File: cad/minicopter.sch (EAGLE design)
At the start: 39 parts, among them CN2 DO NOT PLACE, U1 STM32F411/48, U2 LSM6DS3, U3 DRV8839, U4 LPS25HB, U5 DRV8839, U6 LIS3MDL

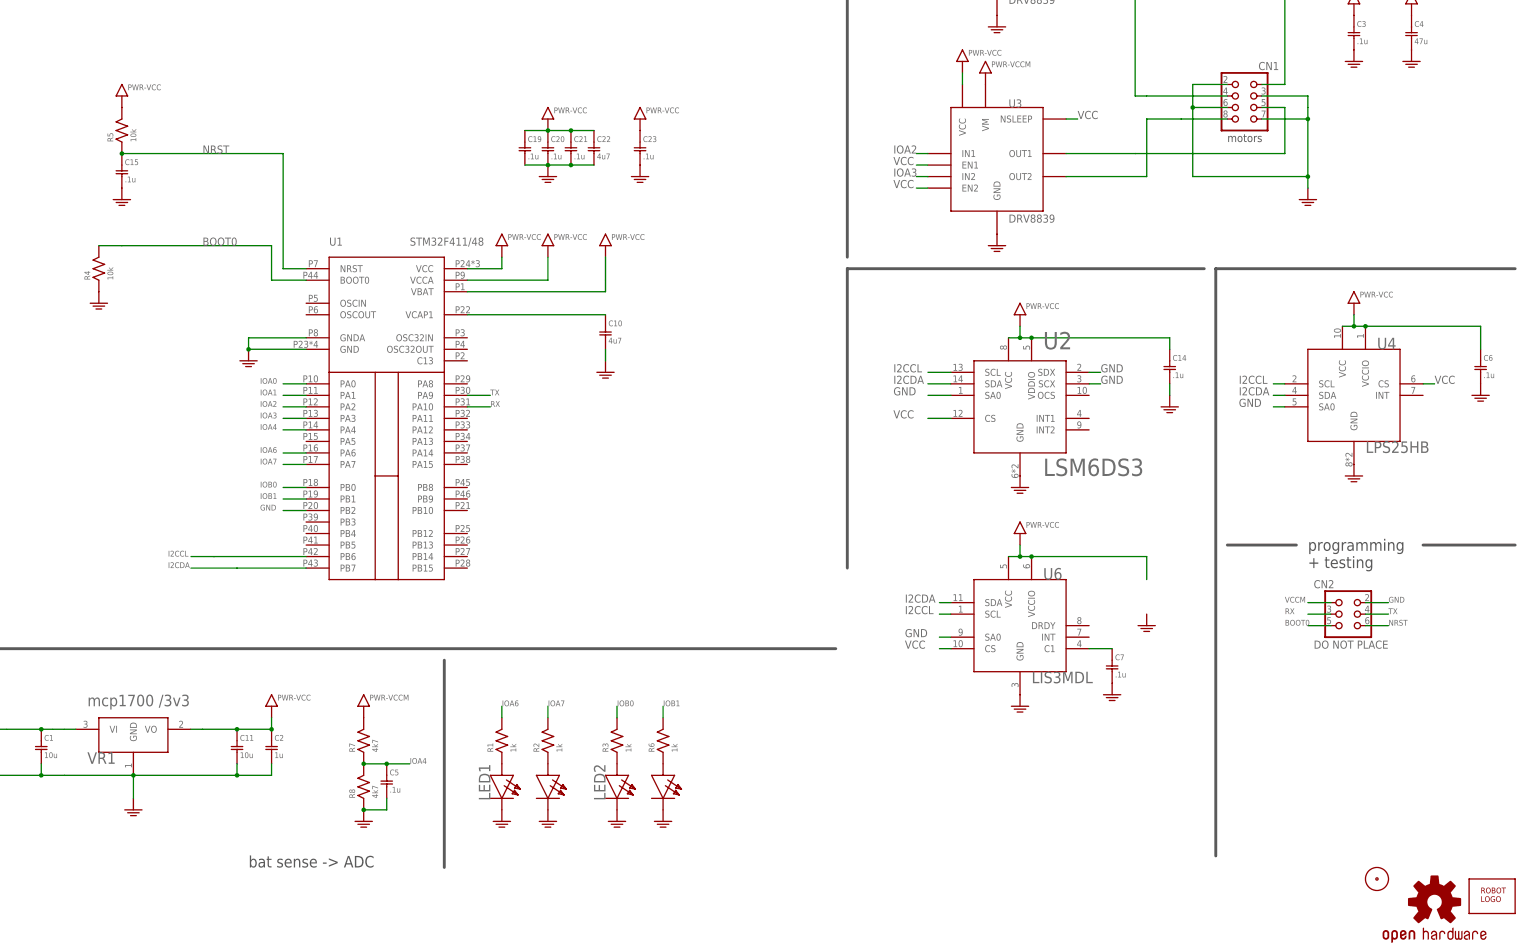
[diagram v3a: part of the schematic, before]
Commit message: add piezo
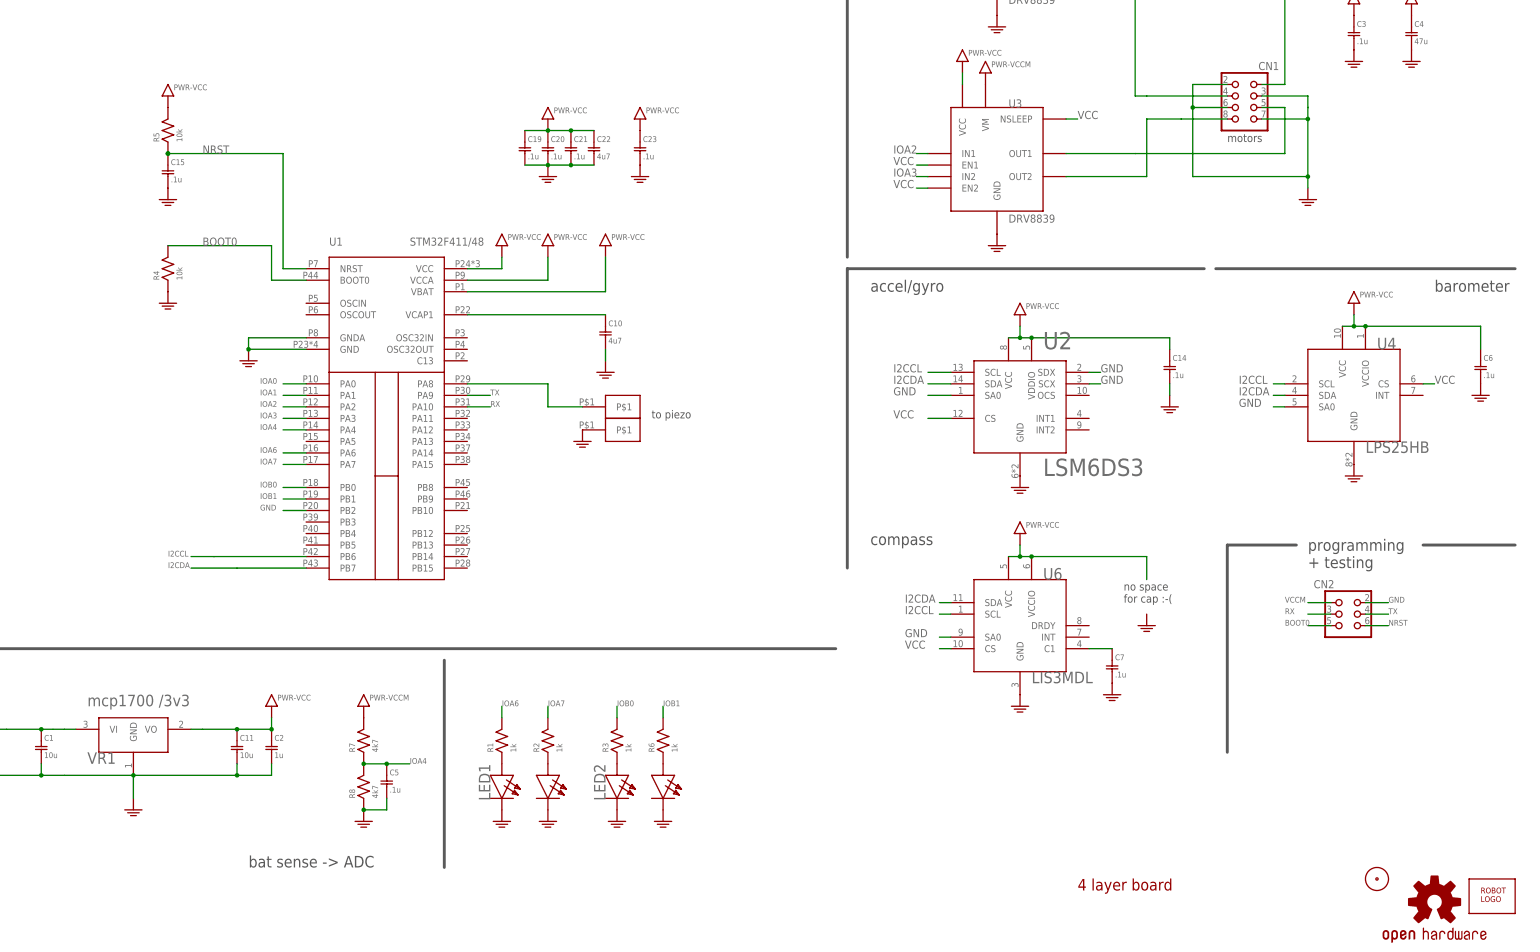
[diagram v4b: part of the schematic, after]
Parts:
- added CN4, CN5: HEADER-1X1SMALL, jaw:HEADER-1X1SMALL
- CN2: value DO NOT PLACE -> HEADER-3X2-PTH
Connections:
- new net PZ0: CN4.P$1, U1.PA8
- net GND: now also CN5.P$1
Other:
- note added: "4 layer board"
- note added: "accel/gyro"
- note added: "barometer"
- note added: "compass"
- note added: "no space for cap :-("
- note added: "to piezo"
- moved on the sheet: C15, R4, R5
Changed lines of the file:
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@@
 <part name="VR1" library="jaw" deviceset="REGULATOR" device="-SOT23-3" value="mcp1700 /3v3"/>
 <part name="FRAME2" library="frames" deviceset="FRAME_B_L" device=""/>
-<part name="CN2" library="jaw" deviceset="HEADER-3X2" device="-PTH" value="DO NOT PLACE"/>
+<part name="CN2" library="jaw" deviceset="HEADER-3X2" device="-PTH" value=""/>
 <part name="CN1" library="jaw" deviceset="HEADER-2X4" device=""/>
 <part name="LED1" library="jaw" deviceset="LED-DUAL" device="0805"/>
@@
 <part name="GND22" library="jaw" deviceset="PWR-GND" device=""/>
 <part name="U$2" library="jaw" deviceset="FIDUCIAL" device=""/>
+<part name="GND23" library="jaw" deviceset="PWR-GND" device=""/>
+<part name="CN4" library="jaw" deviceset="HEADER-1X1" device="SMALL"/>
+<part name="CN5" library="jaw" deviceset="HEADER-1X1" device="SMALL"/>
 </parts>
 <sheets>
@@
 <text x="378.46" y="101.6" size="2.54" layer="97">programming
 + testing</text>
-<wire x1="358.14" y1="38.1" x2="358.14" y2="167.64" width="0.635" layer="97"/>
 <wire x1="358.14" y1="167.64" x2="424.18" y2="167.64" width="0.635" layer="97"/>
 <wire x1="360.68" y1="106.68" x2="375.92" y2="106.68" width="0.635" layer="97"/>
@@
 <text x="144.78" y="35.56" size="2.54" layer="97" ratio="10">bat sense -&gt; ADC</text>
 <text x="360.68" y="195.58" size="1.778" layer="97" ratio="10">motors</text>
+<text x="233.68" y="134.62" size="1.778" layer="97" ratio="10">to piezo</text>
+<text x="337.82" y="93.98" size="1.778" layer="97" ratio="10">no space
+for cap :-(</text>
+<wire x1="360.68" y1="106.68" x2="360.68" y2="60.96" width="0.635" layer="97"/>
+<text x="281.94" y="162.56" size="2.54" layer="97" ratio="10">accel/gyro</text>
+<text x="281.94" y="106.68" size="2.54" layer="97" ratio="10">compass</text>
+<text x="406.4" y="162.56" size="2.54" layer="97" ratio="10">barometer</text>
+<text x="327.66" y="30.48" size="2.54" layer="94" ratio="10">4 layer board</text>
 </plain>
 <instances>
@@
 <instance part="C2" gate="G$1" x="149.86" y="60.96"/>
 <instance part="GND3" gate="G$1" x="119.38" y="48.26"/>
-<instance part="C15" gate="G$1" x="116.84" y="187.96"/>
-<instance part="R4" gate="G$1" x="111.76" y="167.64" rot="R90"/>
-<instance part="R5" gate="G$1" x="116.84" y="198.12" rot="R90"/>
-<instance part="VCC10" gate="G$1" x="116.84" y="205.74"/>
-<instance part="GND16" gate="G$1" x="111.76" y="160.02"/>
-<instance part="GND18" gate="G$1" x="116.84" y="182.88"/>
+<instance part="C15" gate="G$1" x="127" y="187.96"/>
+<instance part="R4" gate="G$1" x="127" y="167.64" rot="R90"/>
+<instance part="R5" gate="G$1" x="127" y="198.12" rot="R90"/>
+<instance part="VCC10" gate="G$1" x="127" y="205.74"/>
+<instance part="GND16" gate="G$1" x="127" y="160.02"/>
+<instance part="GND18" gate="G$1" x="127" y="182.88"/>
 <instance part="C19" gate="G$1" x="205.74" y="193.04"/>
 <instance part="C20" gate="G$1" x="210.82" y="193.04"/>
@@
 <instance part="GND22" gate="G$1" x="342.9" y="88.9"/>
 <instance part="U$2" gate="G$1" x="393.7" y="33.02"/>
+<instance part="GND23" gate="G$1" x="218.44" y="129.54"/>
+<instance part="CN4" gate="G$1" x="226.06" y="137.16"/>
+<instance part="CN5" gate="G$1" x="226.06" y="132.08"/>
 </instances>
 <busses>
@@
 <pinref part="GND21" gate="G$1" pin="GND"/>
 </segment>
+<segment>
+<pinref part="CN5" gate="G$1" pin="P$1"/>
+<pinref part="GND23" gate="G$1" pin="GND"/>
+</segment>
 </net>
 <net name="VCC" class="0">
@@
 <segment>
 <pinref part="R4" gate="G$1" pin="P$2"/>
-<wire x1="116.84" y1="172.72" x2="111.76" y2="172.72" width="0.1524" layer="91"/>
-<wire x1="116.84" y1="172.72" x2="149.86" y2="172.72" width="0.1524" layer="91"/>
+<wire x1="127" y1="172.72" x2="149.86" y2="172.72" width="0.1524" layer="91"/>
 <wire x1="149.86" y1="172.72" x2="149.86" y2="165.1" width="0.1524" layer="91"/>
 <pinref part="U1" gate="G$1" pin="BOOT0"/>
@@
 <pinref part="R5" gate="G$1" pin="P$1"/>
 <pinref part="R5" gate="G$1" pin="P$1"/>
-<junction x="116.84" y="193.04"/>
-<wire x1="116.84" y1="193.04" x2="152.4" y2="193.04" width="0.1524" layer="91"/>
+<junction x="127" y="193.04"/>
+<wire x1="127" y1="193.04" x2="152.4" y2="193.04" width="0.1524" layer="91"/>
 <wire x1="152.4" y1="193.04" x2="152.4" y2="167.64" width="0.1524" layer="91"/>
 <pinref part="U1" gate="G$1" pin="NRST"/>
 <wire x1="152.4" y1="167.64" x2="157.48" y2="167.64" width="0.1524" layer="91"/>
 <label x="134.62" y="193.04" size="1.778" layer="95"/>
+<junction x="127" y="193.04"/>
 </segment>
 <segment>
@@
 </segment>
 </net>
+<net name="PZ0" class="0">
+<segment>
+<pinref part="U1" gate="G$1" pin="PA8"/>
+<wire x1="193.04" y1="142.24" x2="210.82" y2="142.24" width="0.1524" layer="91"/>
+<wire x1="210.82" y1="142.24" x2="210.82" y2="137.16" width="0.1524" layer="91"/>
+<wire x1="210.82" y1="137.16" x2="218.44" y2="137.16" width="0.1524" layer="91"/>
+<pinref part="CN4" gate="G$1" pin="P$1"/>
+</segment>
+</net>
